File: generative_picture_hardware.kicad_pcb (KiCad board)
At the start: 2 copper layers, 100 x 100 mm, 59 parts, among them J1 e_Paper_HAT, J3 USB_C_Receptacle_USB2.0, Q1 PMN48XP, Q2 DMG9926UDM, Q3 MBT3904DW1, U1 AP2112K-3.3, U2 ESP32-WROOM-32, U3 MCP73831-2ACI-OT, U4 AP9101CK6*, U5 FT231XS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

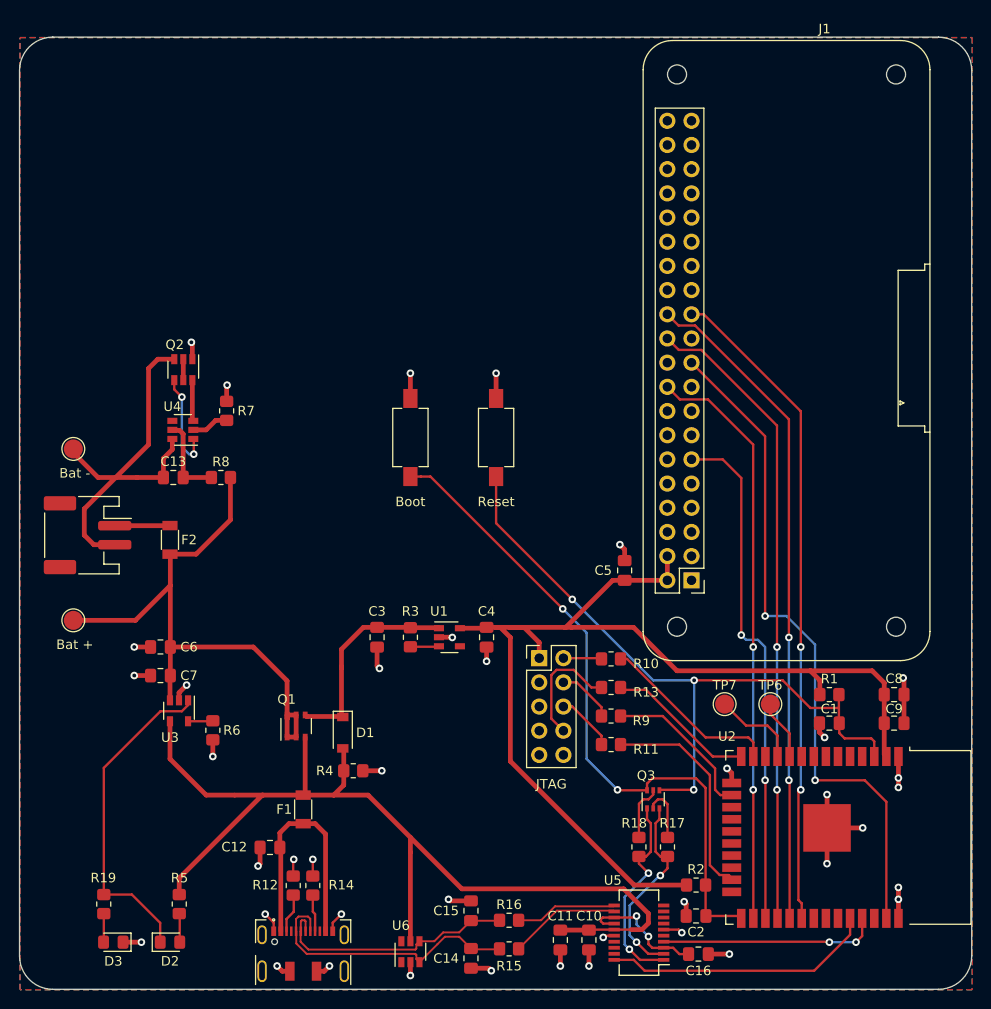
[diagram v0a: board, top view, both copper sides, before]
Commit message: moves JTAG connector so we have more space for the labels
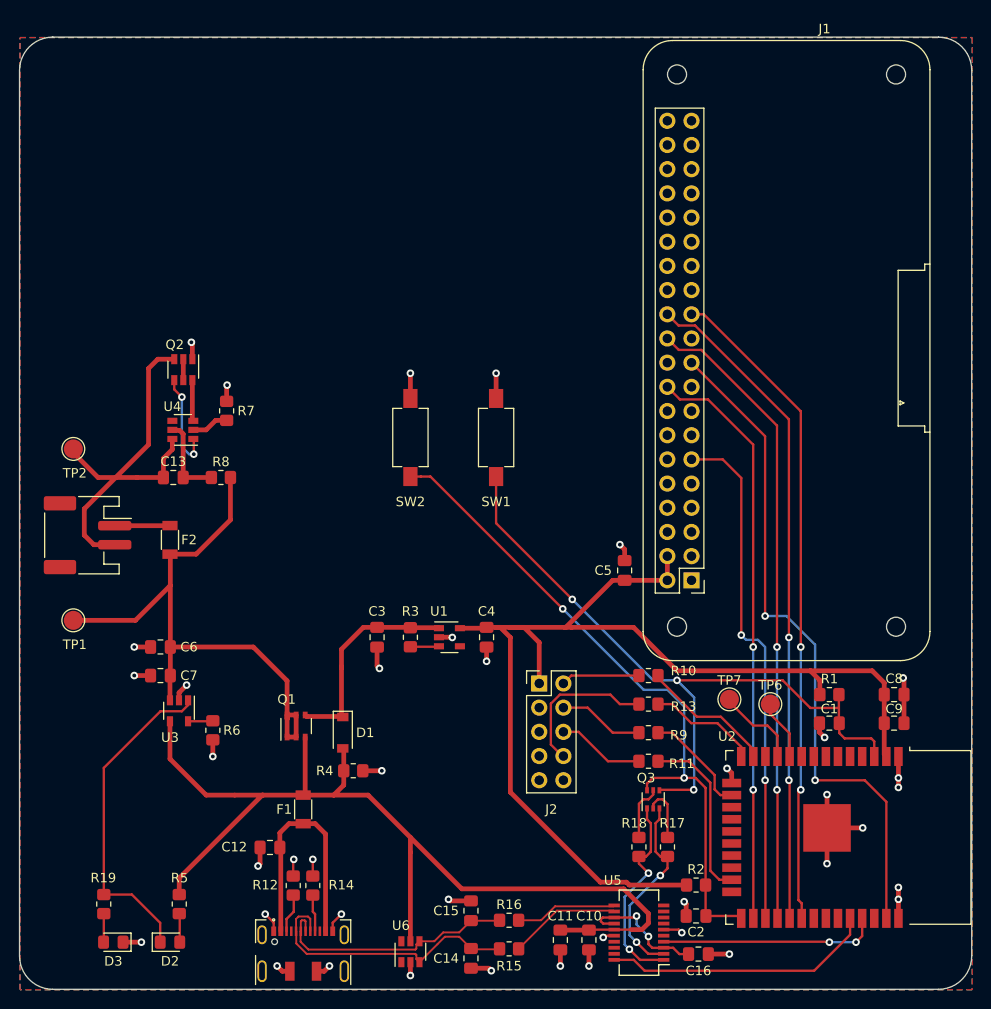
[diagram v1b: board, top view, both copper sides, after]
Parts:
- TP1: renamed from Bat +
- TP2: renamed from Bat -
- moved R10 4.30 mm to (166.0, 119.0)
- moved R11 4.30 mm to (166.0, 128.0)
- moved R13 4.30 mm to (166.0, 122.0)
- moved R9 4.30 mm to (166.0, 125.0)
- moved J2 2.66 mm to (154.5, 119.8)
- moved TP7 0.71 mm to (174.5, 121.5)
- renumbered JTAG to J2, Reset to SW1, Boot to SW2
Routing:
- net MTCK: track 16.4 -> 11.3 mm
- net MTMS: track 19.1 -> 14.1 mm
- net MTDO: track 23.2 -> 18.3 mm
- net +3V3: track 117.4 -> 122.0 mm
- net Net-(J2-Pad2): track 4.03 -> 8.27 mm
- net MTDI: track 15.7 -> 11.6 mm
- net Net-(J2-Pad8): track 12.6 -> 16.2 mm
- net Net-(J2-Pad4): track 6.01 -> 9.02 mm
- net Net-(J2-Pad6): track 6.20 -> 9.21 mm
- net ESP_EN: track 73.8 -> 74.5 mm

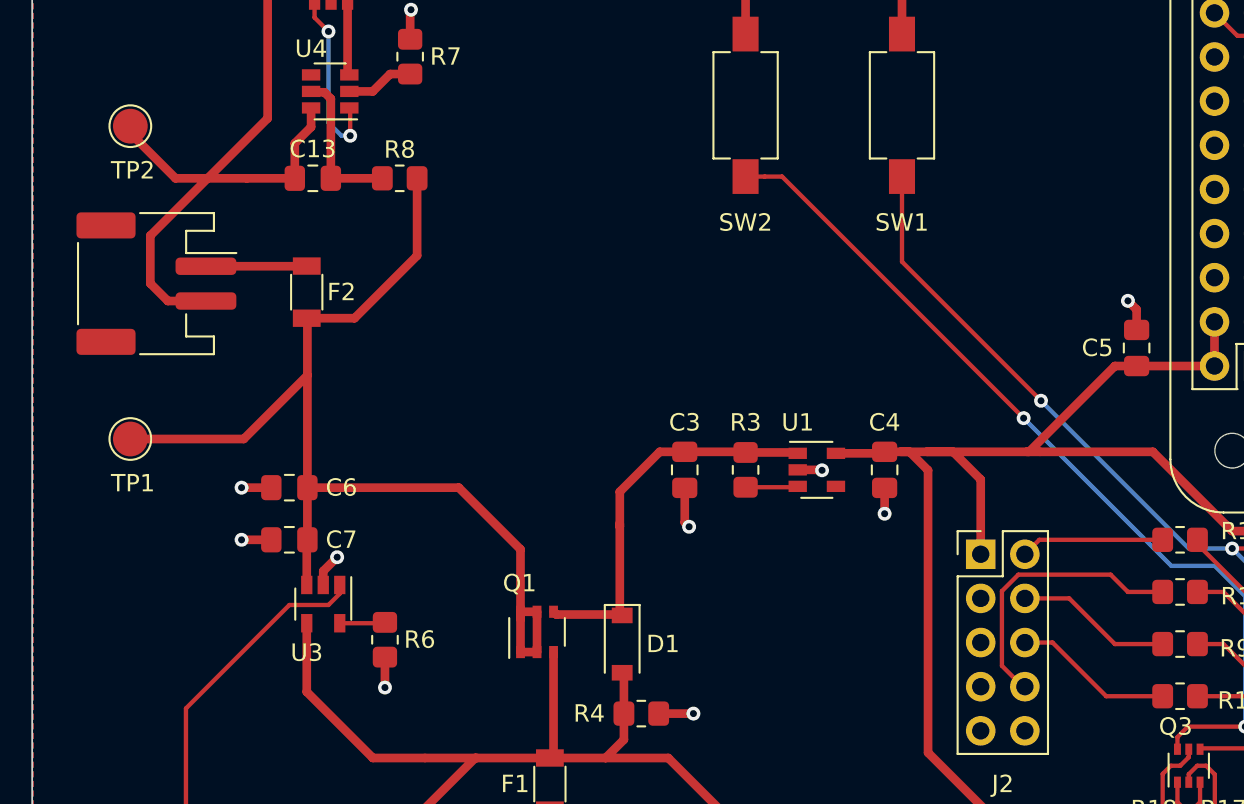
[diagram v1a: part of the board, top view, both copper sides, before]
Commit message: Removes battery test points and adds labels to JTAG connector
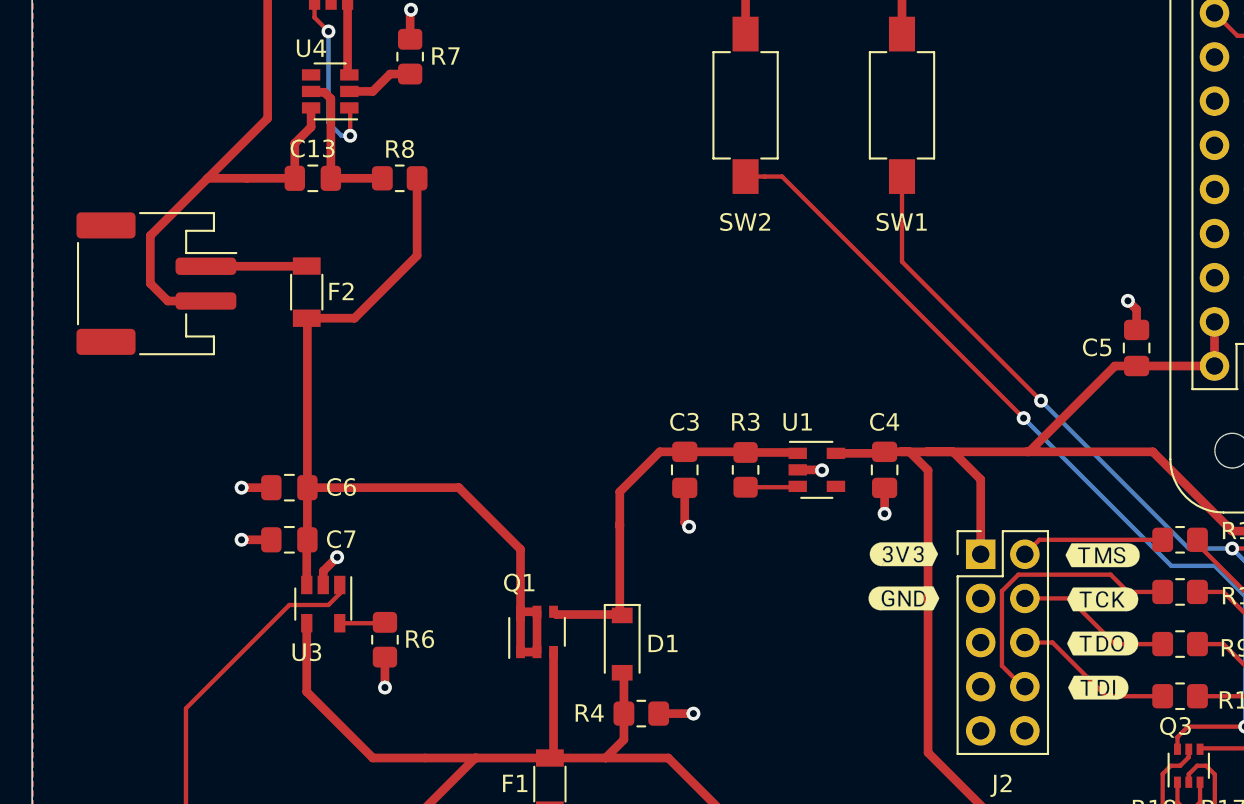
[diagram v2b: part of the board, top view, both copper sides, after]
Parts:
- removed TP1: bat+, TestPoint:TestPoint_Pad_D2.0mm
- removed TP2: bat -, TestPoint:TestPoint_Pad_D2.0mm
- added ?: , buzzardLabel, F.Cu at (150.1, 122.4)
- added ?: , buzzardLabel, F.Cu at (161.5, 125.0)
- added ?: , buzzardLabel, F.Cu at (161.5, 122.4)
- added ?: , buzzardLabel, F.Cu at (150.1, 119.8)
- added ?: , buzzardLabel, F.Cu at (161.3, 127.5)
- added ?: , buzzardLabel, F.Cu at (161.5, 119.9)
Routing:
- net +BATT: track 63.6 -> 51.9 mm
- net Net-(BT1-Pad2): track 42.4 -> 36.5 mm

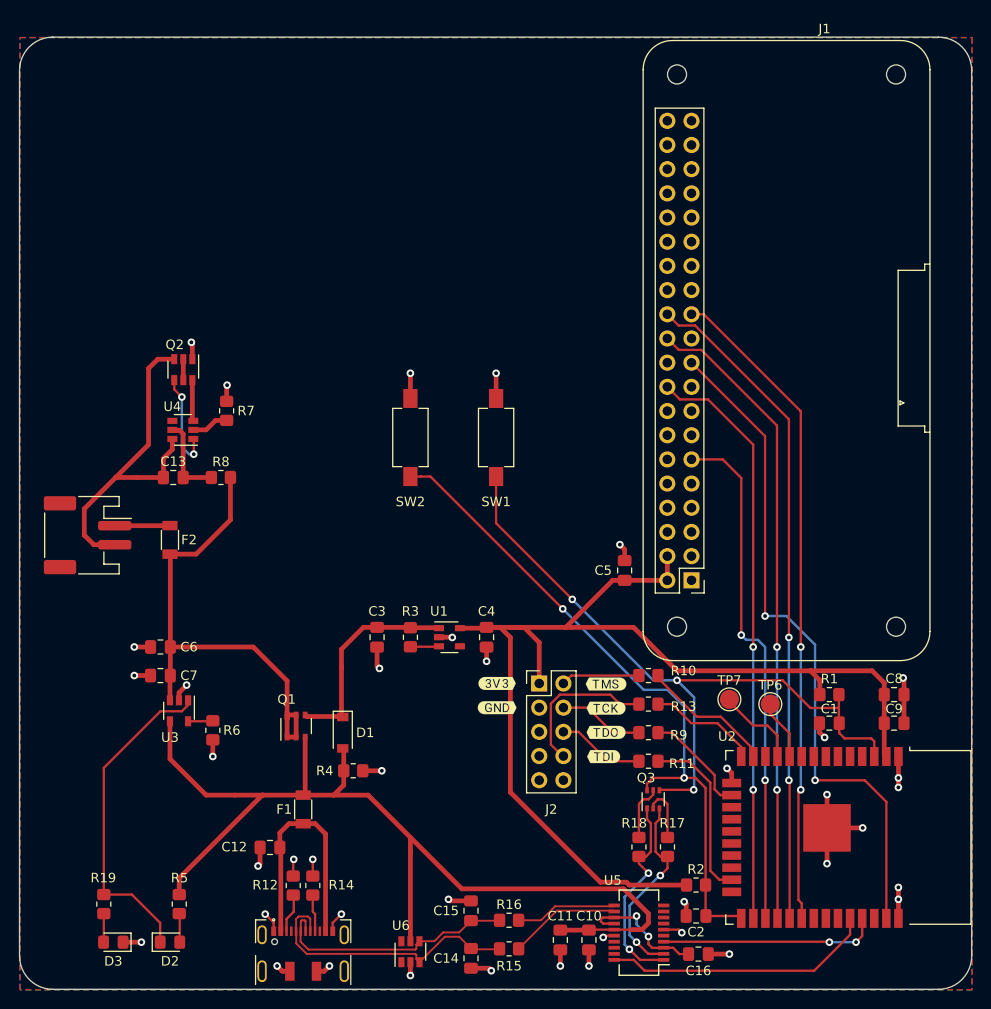
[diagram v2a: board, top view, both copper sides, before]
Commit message: Removes copper fills from below the antenna keepout area
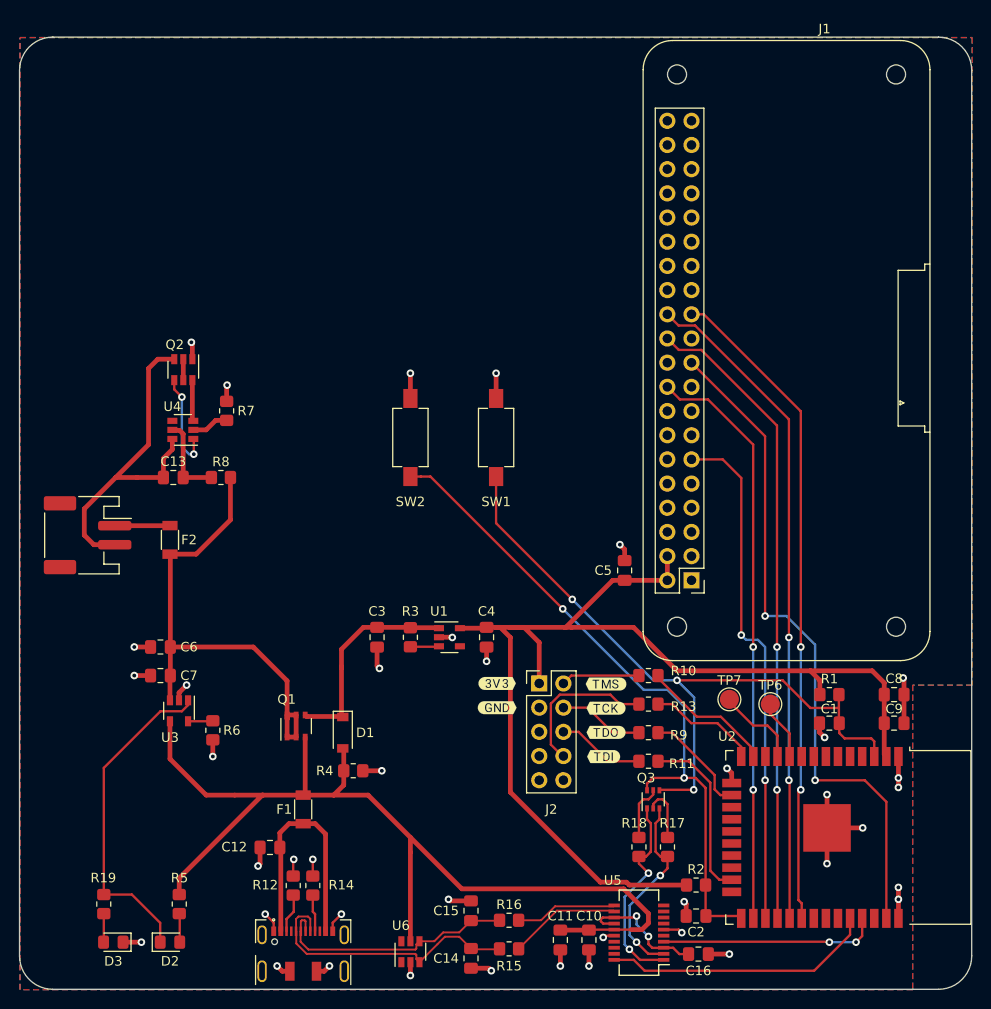
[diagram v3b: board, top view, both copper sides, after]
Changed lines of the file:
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@@
   (segment (start 165.6 150) (end 164.4575 148.8575) (width 0.25) (layer "F.Cu") (net 83))
   (segment (start 164.4575 148.8575) (end 162.4 148.8575) (width 0.25) (layer "F.Cu") (net 83))
-  (zone (net 0) (net_name "") (layers F&B.Cu) (hatch edge 0.508)
-    (connect_pads (clearance 0))
-    (min_thickness 0.254)
-    (keepout (tracks not_allowed) (vias not_allowed) (pads not_allowed ) (copperpour not_allowed) (footprints not_allowed))
-    (fill (thermal_gap 0.508) (thermal_bridge_width 0.508))
-    (polygon
-      (pts
-        (xy 200 160.05)
-        (xy 194 160.05)
-        (xy 194 112)
-        (xy 199.9 112)
-      )
-    )
-  )
   (zone (net 3) (net_name "GND") (layer "F.Cu") (hatch edge 0.508)
     (connect_pads (clearance 0.508))
@@
     (polygon
       (pts
-        (xy 200 152)
+        (xy 200 120)
+        (xy 193.75 120)
+        (xy 193.75 152)
         (xy 100 152)
         (xy 100 52)
@@
     (polygon
       (pts
-        (xy 200 152)
+        (xy 200 120)
+        (xy 193.75 120)
+        (xy 193.75 152)
         (xy 100 152)
         (xy 100 52)

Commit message: Adds some vias to stitch the bottom and top ground planes
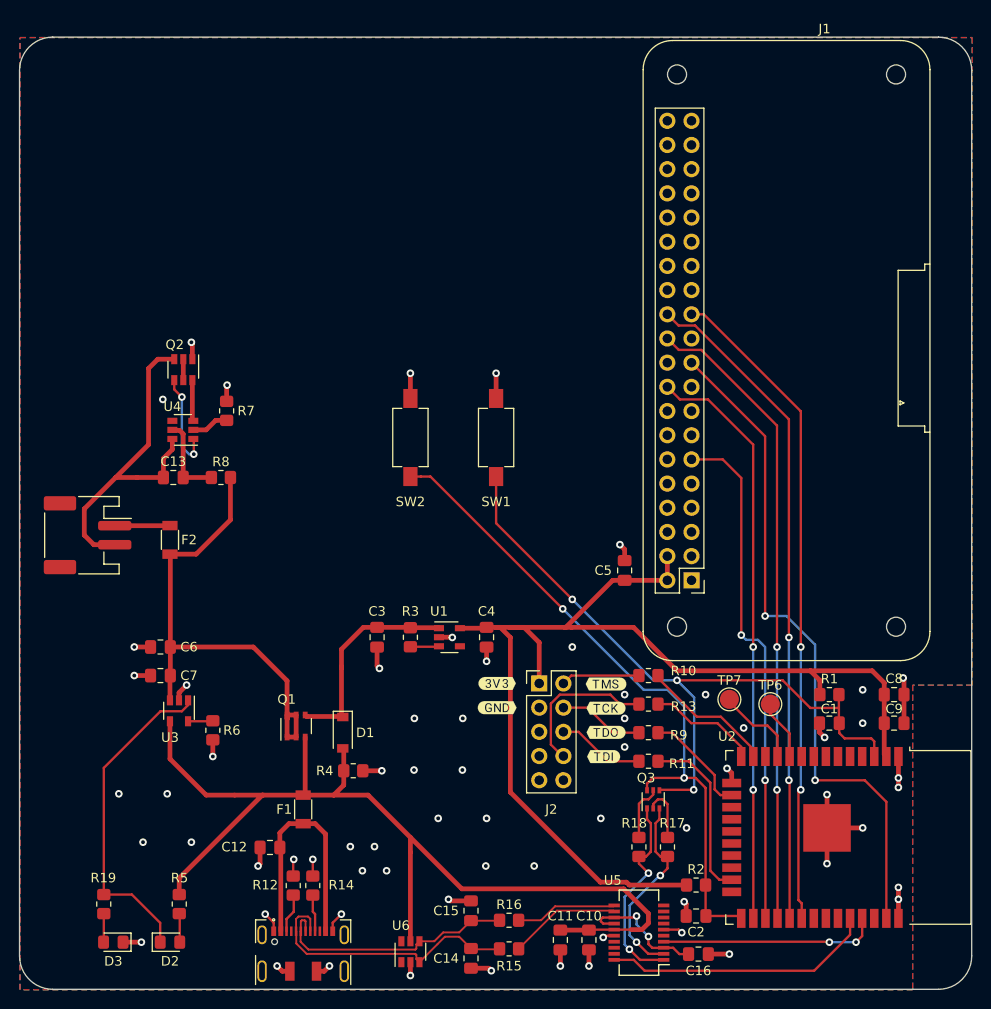
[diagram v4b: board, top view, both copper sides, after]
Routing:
- net GND: vias 40 -> 67
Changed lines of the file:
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@@
   (via (at 117.5 120) (size 0.8) (drill 0.4) (layers "F.Cu" "B.Cu") (net 3))
   (via (at 184.5 125.5) (size 0.8) (drill 0.4) (layers "F.Cu" "B.Cu") (net 3))
+  (via (at 146.46 128.92) (size 0.8) (drill 0.4) (layers "F.Cu" "B.Cu") (free) (net 3))
   (via (at 118 84) (size 0.8) (drill 0.4) (layers "F.Cu" "B.Cu") (net 3))
   (via (at 156.75 149.5) (size 0.8) (drill 0.4) (layers "F.Cu" "B.Cu") (net 3))
+  (via (at 163.5 121) (size 0.8) (drill 0.4) (layers "F.Cu" "B.Cu") (free) (net 3))
+  (via (at 115 90) (size 0.8) (drill 0.4) (layers "F.Cu" "B.Cu") (free) (net 3))
+  (via (at 188.5 120.5) (size 0.8) (drill 0.4) (layers "F.Cu" "B.Cu") (free) (net 3))
   (via (at 112 116) (size 0.8) (drill 0.4) (layers "F.Cu" "B.Cu") (net 3))
   (via (at 120.25 127.5) (size 0.8) (drill 0.4) (layers "F.Cu" "B.Cu") (net 3))
+  (via (at 163.5 126.5) (size 0.8) (drill 0.4) (layers "F.Cu" "B.Cu") (free) (net 3))
+  (via (at 137.23 136.96) (size 0.8) (drill 0.4) (layers "F.Cu" "B.Cu") (free) (net 3))
+  (via (at 176 124.5) (size 0.8) (drill 0.4) (layers "F.Cu" "B.Cu") (free) (net 3))
   (via (at 145.4 115) (size 0.8) (drill 0.4) (layers "F.Cu" "B.Cu") (net 3))
   (via (at 130.75 138.304098) (size 0.8) (drill 0.4) (layers "F.Cu" "B.Cu") (net 3))
+  (via (at 110.38 131.42) (size 0.8) (drill 0.4) (layers "F.Cu" "B.Cu") (free) (net 3))
+  (via (at 161 134) (size 0.8) (drill 0.4) (layers "F.Cu" "B.Cu") (free) (net 3))
   (via (at 128.75 138.304098) (size 0.8) (drill 0.4) (layers "F.Cu" "B.Cu") (net 3))
+  (via (at 143.92 134) (size 0.8) (drill 0.4) (layers "F.Cu" "B.Cu") (free) (net 3))
+  (via (at 148.92 139) (size 0.8) (drill 0.4) (layers "F.Cu" "B.Cu") (free) (net 3))
   (via (at 132.5 149.5) (size 0.8) (drill 0.4) (layers "F.Cu" "B.Cu") (net 3))
   (via (at 127 149.5) (size 0.8) (drill 0.4) (layers "F.Cu" "B.Cu") (net 3))
+  (via (at 112.92 136.5) (size 0.8) (drill 0.4) (layers "F.Cu" "B.Cu") (free) (net 3))
+  (via (at 163.5 123.5) (size 0.8) (drill 0.4) (layers "F.Cu" "B.Cu") (free) (net 3))
   (via (at 133.75 144.054098) (size 0.8) (drill 0.4) (layers "F.Cu" "B.Cu") (net 3))
   (via (at 150 87.25) (size 0.8) (drill 0.4) (layers "F.Cu" "B.Cu") (net 3))
+  (via (at 149 134) (size 0.8) (drill 0.4) (layers "F.Cu" "B.Cu") (free) (net 3))
   (via (at 149 117.5) (size 0.8) (drill 0.4) (layers "F.Cu" "B.Cu") (net 3))
+  (via (at 141.38 128.92) (size 0.8) (drill 0.4) (layers "F.Cu" "B.Cu") (free) (net 3))
+  (via (at 115.46 131.42) (size 0.8) (drill 0.4) (layers "F.Cu" "B.Cu") (free) (net 3))
+  (via (at 134.69 136.96) (size 0.8) (drill 0.4) (layers "F.Cu" "B.Cu") (free) (net 3))
   (via (at 192.75 119.25) (size 0.8) (drill 0.4) (layers "F.Cu" "B.Cu") (net 3))
   (via (at 141 87.25) (size 0.8) (drill 0.4) (layers "F.Cu" "B.Cu") (net 3))
@@
   (via (at 137.75 118.25) (size 0.8) (drill 0.4) (layers "F.Cu" "B.Cu") (net 3))
   (via (at 141 150.5) (size 0.8) (drill 0.4) (layers "F.Cu" "B.Cu") (net 3))
+  (via (at 158 116) (size 0.8) (drill 0.4) (layers "F.Cu" "B.Cu") (free) (net 3))
   (via (at 192.25 130.75) (size 0.8) (drill 0.4) (layers "F.Cu" "B.Cu") (net 3))
+  (via (at 170 135) (size 0.8) (drill 0.4) (layers "F.Cu" "B.Cu") (free) (net 3))
+  (via (at 118 136.5) (size 0.8) (drill 0.4) (layers "F.Cu" "B.Cu") (free) (net 3))
   (via (at 149.5 150) (size 0.8) (drill 0.4) (layers "F.Cu" "B.Cu") (net 3))
+  (via (at 172 121) (size 0.8) (drill 0.4) (layers "F.Cu" "B.Cu") (free) (net 3))
   (via (at 159.75 149.5) (size 0.8) (drill 0.4) (layers "F.Cu" "B.Cu") (net 3))
   (via (at 112.75 147) (size 0.8) (drill 0.4) (layers "F.Cu" "B.Cu") (net 3))
+  (via (at 135.96 139.5) (size 0.8) (drill 0.4) (layers "F.Cu" "B.Cu") (free) (net 3))
+  (via (at 146.5 123.5) (size 0.8) (drill 0.4) (layers "F.Cu" "B.Cu") (free) (net 3))
   (via (at 138 129) (size 0.8) (drill 0.4) (layers "F.Cu" "B.Cu") (net 3))
   (via (at 145 142.5) (size 0.8) (drill 0.4) (layers "F.Cu" "B.Cu") (net 3))
@@
   (via (at 192.25 142.5) (size 0.8) (drill 0.4) (layers "F.Cu" "B.Cu") (net 3))
   (via (at 125 139) (size 0.8) (drill 0.4) (layers "F.Cu" "B.Cu") (net 3))
+  (via (at 138.5 139.5) (size 0.8) (drill 0.4) (layers "F.Cu" "B.Cu") (free) (net 3))
   (via (at 174.25 128.75) (size 0.8) (drill 0.4) (layers "F.Cu" "B.Cu") (net 3))
+  (via (at 141.42 123.5) (size 0.8) (drill 0.4) (layers "F.Cu" "B.Cu") (free) (net 3))
   (via (at 192.25 141.25) (size 0.8) (drill 0.4) (layers "F.Cu" "B.Cu") (net 3))
   (via (at 188.5 135) (size 0.8) (drill 0.4) (layers "F.Cu" "B.Cu") (net 3))
   (via (at 192.25 129.75) (size 0.8) (drill 0.4) (layers "F.Cu" "B.Cu") (net 3))
   (via (at 125.75 144.054098) (size 0.8) (drill 0.4) (layers "F.Cu" "B.Cu") (net 3))
+  (via (at 188.5 124) (size 0.8) (drill 0.4) (layers "F.Cu" "B.Cu") (free) (net 3))
   (via (at 184.75 138.75) (size 0.8) (drill 0.4) (layers "F.Cu" "B.Cu") (net 3))
   (via (at 169.75 142.75) (size 0.8) (drill 0.4) (layers "F.Cu" "B.Cu") (net 3))
   (via (at 161.25 146.5) (size 0.8) (drill 0.4) (layers "F.Cu" "B.Cu") (net 3))
   (via (at 174.5 148.25) (size 0.8) (drill 0.4) (layers "F.Cu" "B.Cu") (net 3))
+  (via (at 154 139) (size 0.8) (drill 0.4) (layers "F.Cu" "B.Cu") (free) (net 3))
   (segment (start 186 122.4) (end 186 123.9625) (width 0.25) (layer "F.Cu") (net 4))
   (segment (start 167.2 131) (end 167.15 131.05) (width 0.25) (layer "F.Cu") (net 4))
